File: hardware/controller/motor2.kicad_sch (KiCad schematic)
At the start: 51 parts, among them J4 Conn_01x01, J5 Conn_01x01, J6 Conn_01x01, Q2 YJD60N04A, Q3 YJD60N04A, Q4 YJD60N04A, Q5 YJD60N04A, Q6 YJD60N04A, Q7 YJD60N04A, U10 LMV331, U11 LM2105D, U12 LMV331, U13 LM2105D, U14 LMV331, U9 LM2105D

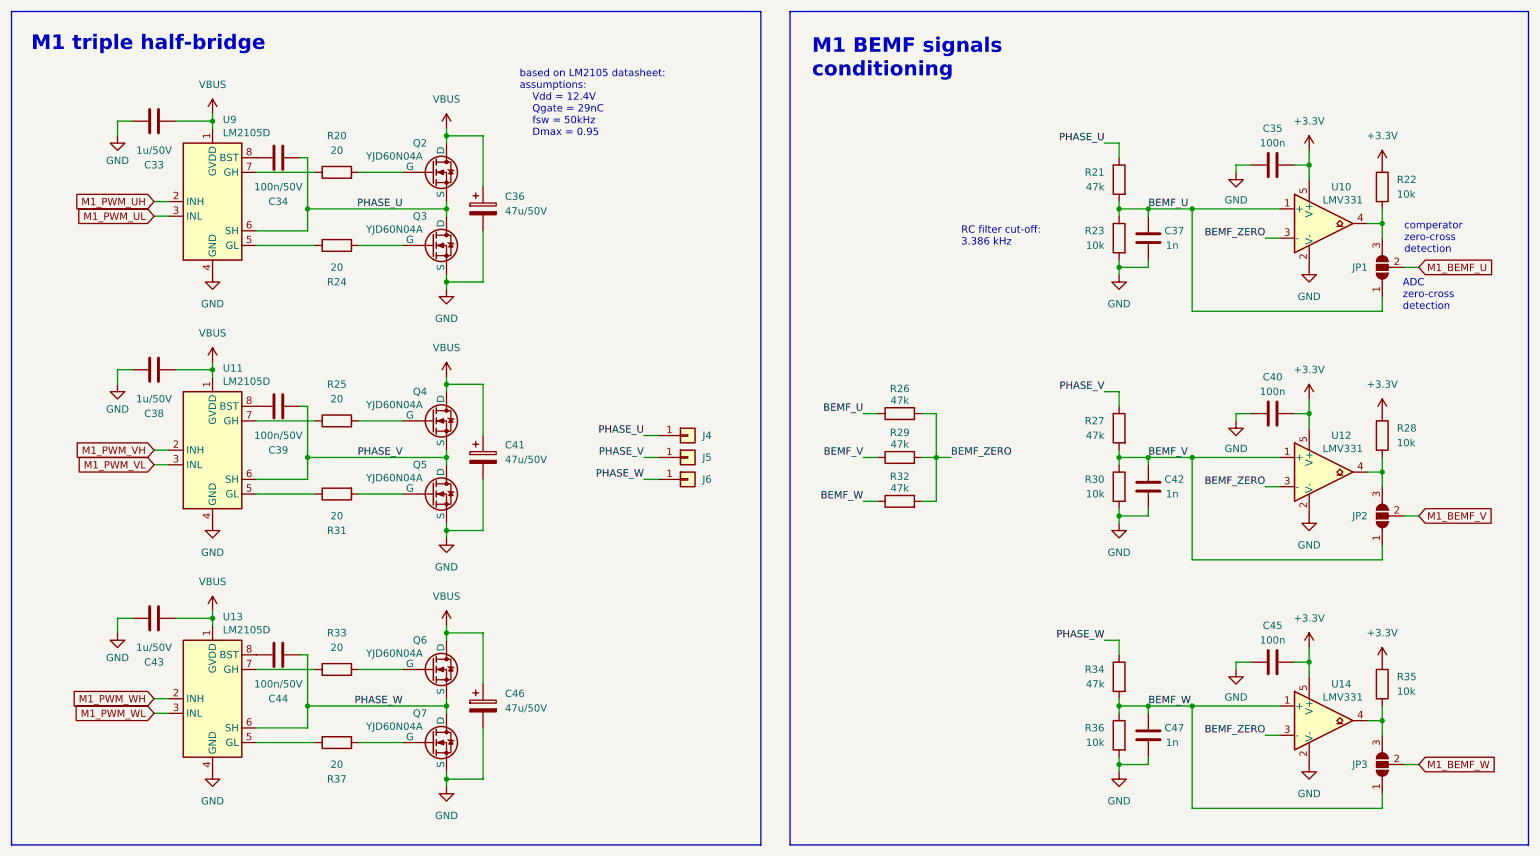
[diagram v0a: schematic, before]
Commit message: uC pinout and second power stage
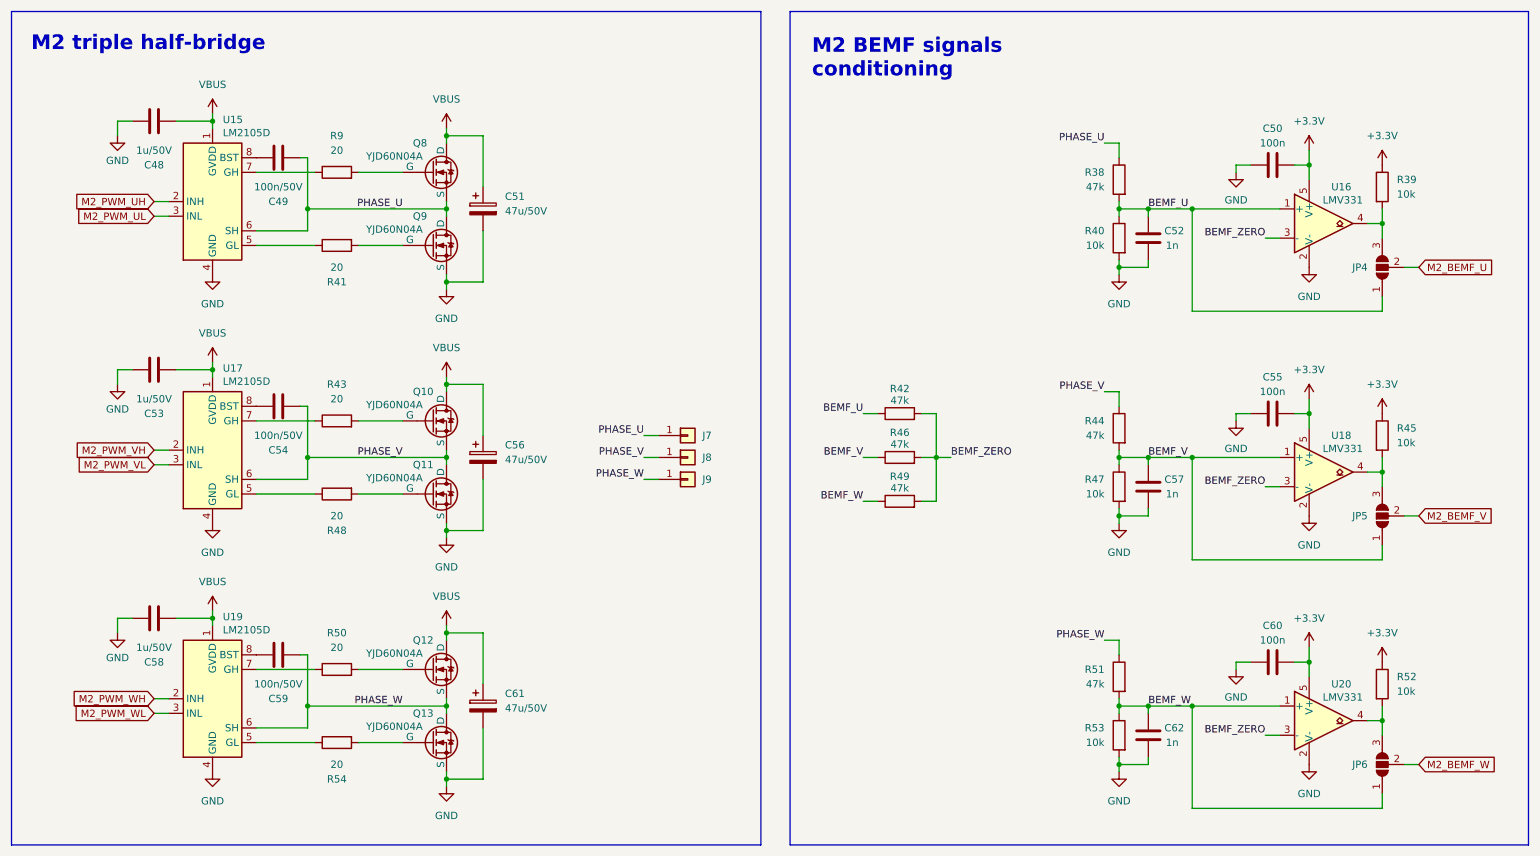
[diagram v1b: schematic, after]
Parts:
- removed C33, C38, C43: 1u/50V, symbol Device:C
- removed C34, C39, C44: 100n/50V, symbol Device:C
- removed C35, C40, C45: 100n, symbol Device:C
- removed C36, C41, C46: 47u/50V, symbol Device:C_Polarized
- removed C37, C42, C47: 1n, symbol Device:C
- removed J4, J5, J6: Conn_01x01, symbol Connector_Generic:Conn_01x01
- removed JP1, JP2, JP3: SolderJumper_3_Open, symbol Jumper:SolderJumper_3_Open
- removed Q2, Q3, Q4, Q5, Q6, Q7: YJD60N04A, symbol Simulation_SPICE:NMOS
- removed R20, R24, R25, R31, R33, R37: 20, symbol Device:R
- removed R21, R26, R27, R29, R32, R34: 47k, symbol Device:R
- removed R22, R23, R28, R30, R35, R36: 10k, symbol Device:R
- removed U10, U12, U14: LMV331, symbol Comparator:LMV331
- removed U11, U13, U9: LM2105D, Package_SO:SOIC-8_3.9x4.9mm_P1.27mm, symbol Driver_FET:LM2105D
- added C48, C53, C58: 1u/50V, symbol Device:C
- added C49, C54, C59: 100n/50V, symbol Device:C
- added C50, C55, C60: 100n, symbol Device:C
- added C51, C56, C61: 47u/50V, symbol Device:C_Polarized
- added C52, C57, C62: 1n, symbol Device:C
- added J7, J8, J9: Conn_01x01, symbol Connector_Generic:Conn_01x01
- added JP4, JP5, JP6: SolderJumper_3_Open, symbol Jumper:SolderJumper_3_Open
- added Q10, Q11, Q12, Q13, Q8, Q9: YJD60N04A, symbol Simulation_SPICE:NMOS
- added R38, R42, R44, R46, R49, R51: 47k, symbol Device:R
- added R39, R40, R45, R47, R52, R53: 10k, symbol Device:R
- added R41, R43, R48, R50, R54, R9: 20, symbol Device:R
- added U15, U17, U19: LM2105D, Package_SO:SOIC-8_3.9x4.9mm_P1.27mm, symbol Driver_FET:LM2105D
- added U16, U18, U20: LMV331, symbol Comparator:LMV331
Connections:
- net +3.3V: now also C50.2, C55.2, C60.2, R39.1, R45.1, R52.1, U16.5 (V+), U18.5 (V+), U20.5 (V+)
- net BEMF_U: now also C52.1, JP4.1 (A), R38.2, R40.1, R42.1, U16.1 (+)
- net BEMF_V: now also C57.1, JP5.1 (A), R44.2, R46.1, R47.1, U18.1 (+)
- net BEMF_W: now also C62.1, JP6.1 (A), R49.1, R51.2, R53.1, U20.1 (+)
- net BEMF_ZERO: now also R42.2, R46.2, R49.2, U16.3 (-), U18.3 (-), U20.3 (-)
- net GND: now also C48.1, C50.1, C51.2, C52.2, C53.1, C55.1, C56.2, C57.2, C58.1, C60.1, C61.2, C62.2, Q11.3 (S), Q13.3 (S), Q9.3 (S), R40.2, R47.2, R53.2, U15.4 (GND), U16.2 (V-), U17.4 (GND), U18.2 (V-), U19.4 (GND), U20.2 (V-)
- net PHASE_U: now also C49.2, J7.1 (Pin_1), Q8.3 (S), Q9.1 (D), R38.1, U15.6 (SH)
- net PHASE_V: now also C54.2, J8.1 (Pin_1), Q10.3 (S), Q11.1 (D), R44.1, U17.6 (SH)
- net PHASE_W: now also C59.2, J9.1 (Pin_1), Q12.3 (S), Q13.1 (D), R51.1, U19.6 (SH)
- net VBUS: now also C48.2, C51.1, C53.2, C56.1, C58.2, C61.1, Q10.1 (D), Q12.1 (D), Q8.1 (D), U15.1 (GVDD), U17.1 (GVDD), U19.1 (GVDD)
- new net: Q12.2 (G), R50.2
- new net: R50.1, U19.7 (GH)
- new net: R41.1, U15.5 (GL)
- new net: R9.1, U15.7 (GH)
- new net: C49.1, U15.8 (BST)
- new net: R43.1, U17.7 (GH)
- new net: Q10.2 (G), R43.2
- new net: JP6.3 (B), R52.2, U20.4
- new net: R54.1, U19.5 (GL)
- new net: C59.1, U19.8 (BST)
- new net: JP4.3 (B), R39.2, U16.4
- new net: Q9.2 (G), R41.2
- new net: Q8.2 (G), R9.2
- new net: R48.1, U17.5 (GL)
- new net: C54.1, U17.8 (BST)
- new net: JP5.3 (B), R45.2, U18.4
- new net: Q13.2 (G), R54.2
- new net: Q11.2 (G), R48.2
- new net M2_BEMF_U: JP4.2 (C)
- new net M2_BEMF_V: JP5.2 (C)
- new net M2_BEMF_W: JP6.2 (C)
- new net M2_PWM_UH: U15.2 (INH)
- new net M2_PWM_UL: U15.3 (INL)
- new net M2_PWM_VH: U17.2 (INH)
- new net M2_PWM_VL: U17.3 (INL)
- new net M2_PWM_WH: U19.2 (INH)
- new net M2_PWM_WL: U19.3 (INL)
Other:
- note added: "M2 BEMF signals conditioning"
- note added: "M2 triple half-bridge"
- note removed: "ADC zero-cross detection"
- note removed: "M1 BEMF signals conditioning"
- note removed: "M1 triple half-bridge"
- note removed: "RC filter cut-off: 3.386 kHz"
- note removed: "based on LM2105 datasheet: assumptions: Vdd = 12.4V Qgate = 29nC fsw = 50kHz Dmax = 0.95"
- note removed: "comperator zero-cross detection"
